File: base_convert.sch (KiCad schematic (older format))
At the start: 53 parts, among them SW1 SW_Push, SW10 SW_Push, SW11 SW_Push, SW12 SW_Push, SW13 SW_Push, SW14 SW_Push, SW15 SW_Push, SW16 SW_Push, SW17 SW_Push, SW18 SW_Push, SW19 SW_Push, SW2 SW_Push, SW20 SW_Push, SW21 SW_Push, SW22 SW_Push, SW23 SW_Push, SW24 SW_Push, SW25 SW_Push, SW26 SW_Push, SW27 SW_Push, SW28 SW_Push, SW29 SW_Push, SW3 SW_Push, SW30 SW_Push, SW31 SW_Push, SW32 SW_Push, SW4 SW_Push, SW5 SW_Push, SW6 SW_Push, SW7 SW_Push, SW8 SW_Push, SW9 SW_Push

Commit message: start schematic
getting there
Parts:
- removed AFF1, AFF2, AFF3, AFF4, AFF5: DA04-11, Displays_7-Segment:DA04-11SURKWA, symbol DA04-11
- removed D1, D10, D11, D12, D13, D14, D15, D16, D2, D3, D4, D5, D6, D7, D8, D9: LED, LEDs:LED_D3.0mm, symbol LED
- removed SW1, SW10, SW11, SW12, SW13, SW14, SW15, SW16, SW17, SW18, SW19, SW2, SW20, SW21, SW22, SW23, SW24, SW25, SW26, SW27, SW28, SW29, SW3, SW30, SW31, SW32, SW4, SW5, SW6, SW7, SW8, SW9: SW_Push, Buttons_Switches_SMD:SW_SPST_FSMSM, symbol SW_Push

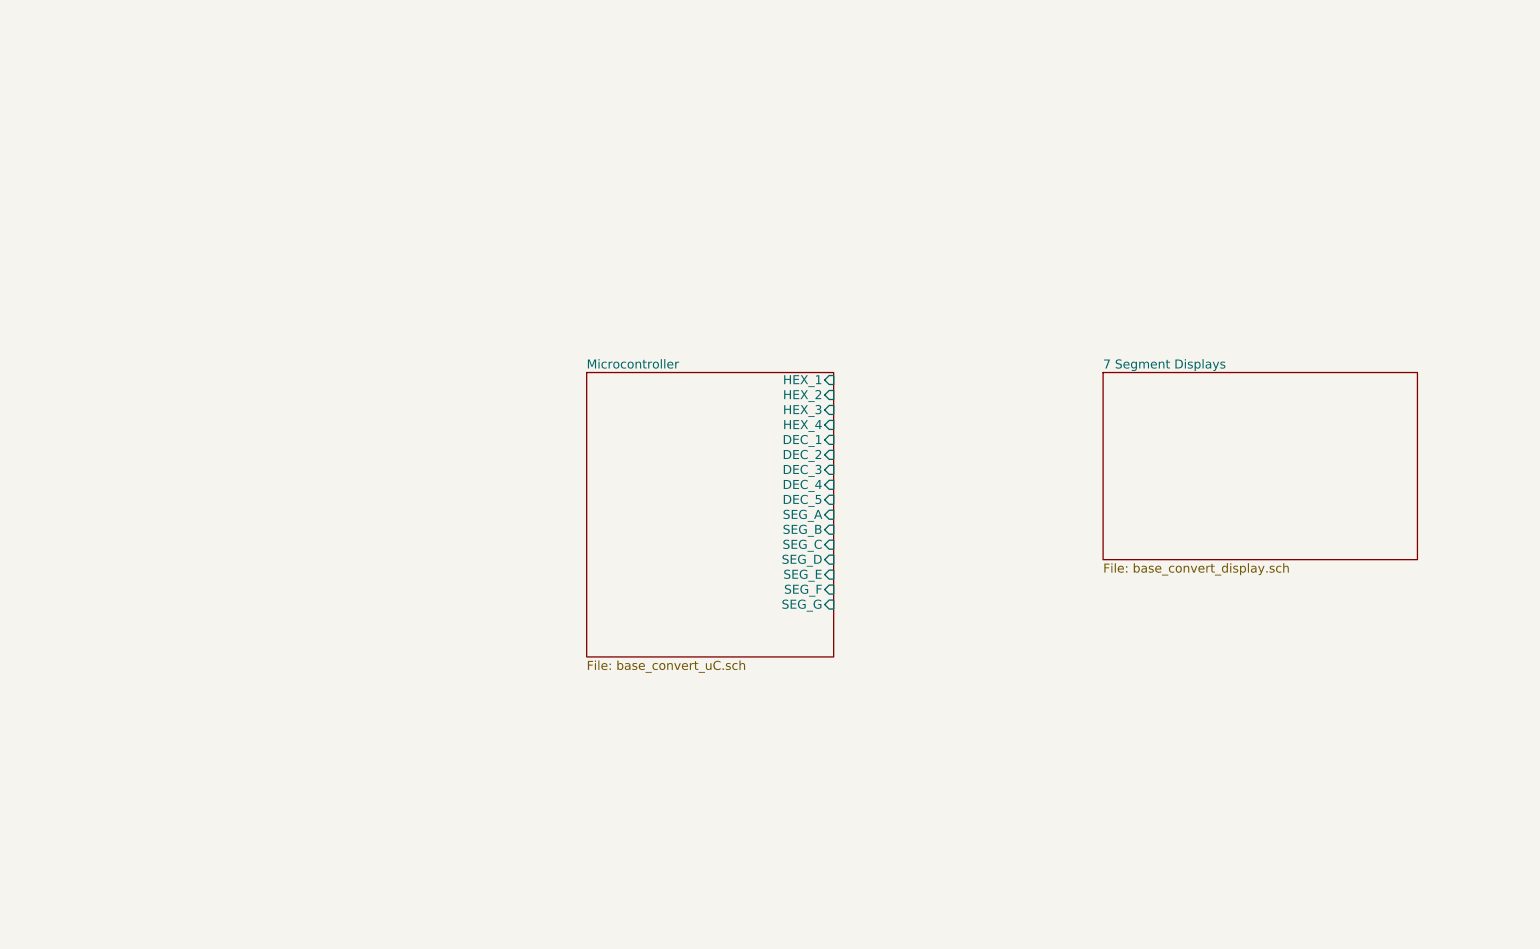
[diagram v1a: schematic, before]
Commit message: capture keypad inputs
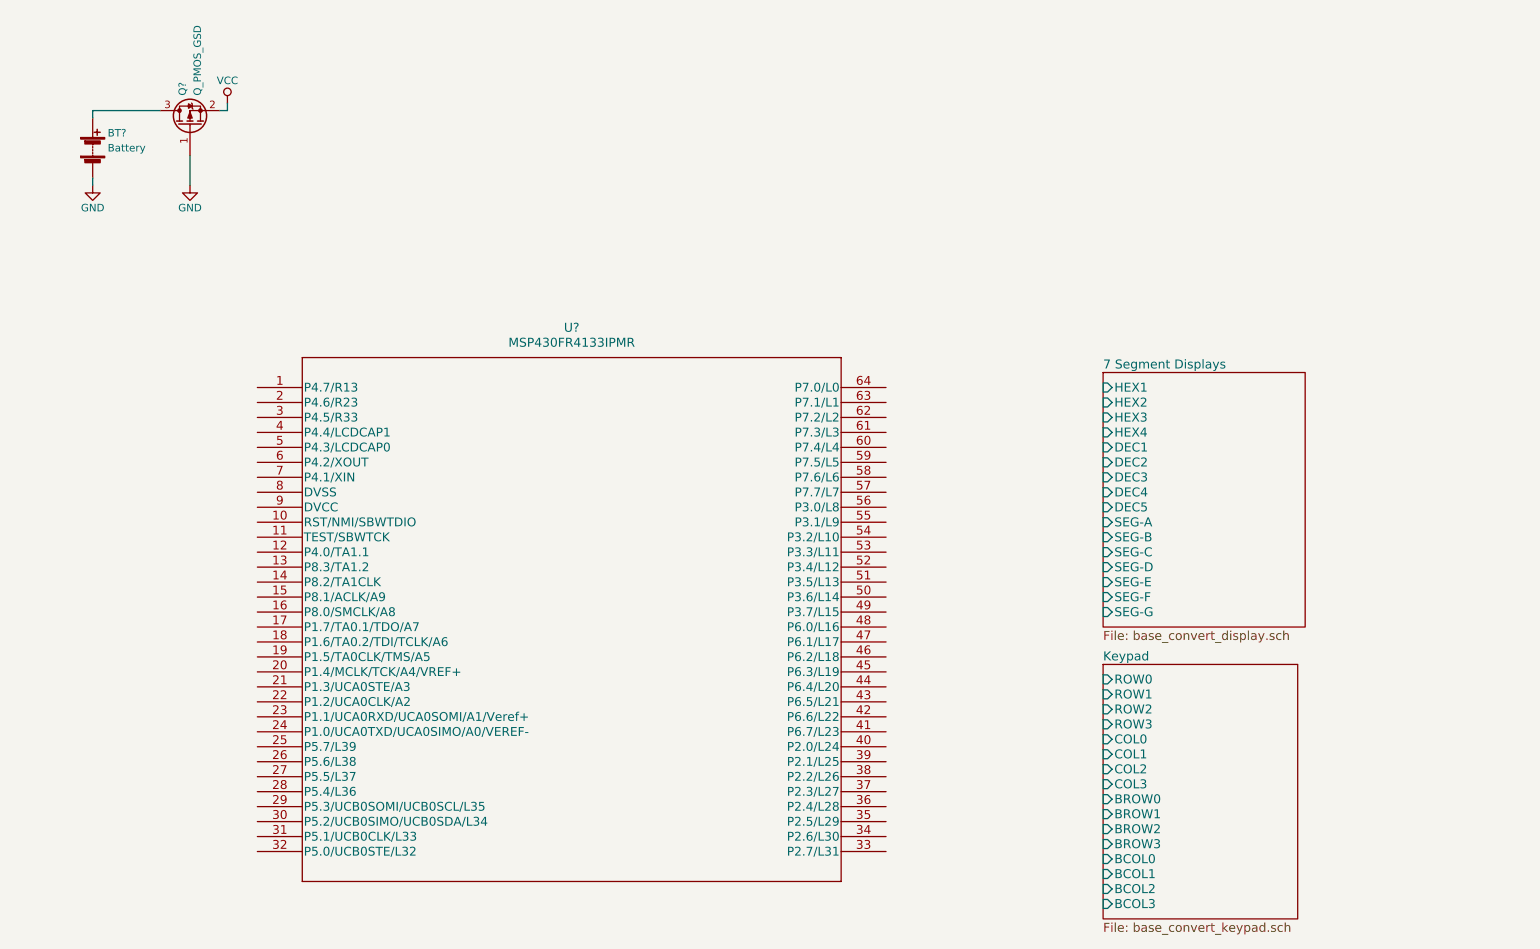
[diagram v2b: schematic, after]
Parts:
- added BT?: Battery, symbol Battery
- added Q?: Q_PMOS_GSD, symbol Q_PMOS_GSD
- added U?: MSP430FR4133IPMR, PM64, symbol MSP430FR4133IPMR
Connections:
- new net: BT?.1 (+), Q?.3 (D)
- new net GND: BT?.2 (-), Q?.1 (G)
- new net VCC: Q?.2 (S)
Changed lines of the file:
@@
 $EndDescr
 $Sheet
-S 4300 2850 1650 1900
-U 5AEA74A7
-F0 "Microcontroller" 60
-F1 "base_convert_uC.sch" 60
-F2 "SEG_A" I R 5950 3800 60
-F3 "SEG_B" I R 5950 3900 60
-F4 "SEG_C" I R 5950 4000 60
-F5 "SEG_D" I R 5950 4100 60
-F6 "SEG_E" I R 5950 4200 60
-F7 "SEG_F" I R 5950 4300 60
-F8 "SEG_G" I R 5950 4400 60
-F9 "HEX_1" I R 5950 2900 60
-F10 "HEX_2" I R 5950 3000 60
-F11 "HEX_3" I R 5950 3100 60
-F12 "HEX_4" I R 5950 3200 60
-F13 "DEC_1" I R 5950 3300 60
-F14 "DEC_2" I R 5950 3400 60
-F15 "DEC_3" I R 5950 3500 60
-F16 "DEC_4" I R 5950 3600 60
-F17 "DEC_5" I R 5950 3700 60
-$EndSheet
-$Sheet
-S 7750 2850 2100 1250
+S 7750 2850 1350 1700
 U 5AEA74C1
 F0 "7 Segment Displays" 60
 F1 "base_convert_display.sch" 60
+F2 "HEX1" I L 7750 2950 60
+F3 "HEX2" I L 7750 3050 60
+F4 "HEX3" I L 7750 3150 60
+F5 "HEX4" I L 7750 3250 60
+F6 "DEC1" I L 7750 3350 60
+F7 "DEC2" I L 7750 3450 60
+F8 "DEC3" I L 7750 3550 60
+F9 "DEC4" I L 7750 3650 60
+F10 "DEC5" I L 7750 3750 60
+F11 "SEG-A" I L 7750 3850 60
+F12 "SEG-B" I L 7750 3950 60
+F13 "SEG-C" I L 7750 4050 60
+F14 "SEG-D" I L 7750 4150 60
+F15 "SEG-E" I L 7750 4250 60
+F16 "SEG-F" I L 7750 4350 60
+F17 "SEG-G" I L 7750 4450 60
+$EndSheet
+$Comp
+L MSP430FR4133IPMR U?
+U 1 1 5AEBBA05
+P 2100 2950
+F 0 "U?" H 4200 3350 60  0000 C CNN
+F 1 "MSP430FR4133IPMR" H 4200 3250 60  0000 C CNN
+F 2 "PM64" H 4200 3190 60  0001 C CNN
+F 3 "" H 2100 2950 60  0000 C CNN
+	1    2100 2950
+	1    0    0    -1
+$EndComp
+$Comp
+L Battery BT?
+U 1 1 5AEC3A00
+P 1000 1350
+F 0 "BT?" H 1100 1450 50  0000 L CNN
+F 1 "Battery" H 1100 1350 50  0000 L CNN
+F 2 "" V 1000 1410 50  0001 C CNN
+F 3 "" V 1000 1410 50  0001 C CNN
+	1    1000 1350
+	1    0    0    -1
+$EndComp
+$Comp
+L GND #PWR?
+U 1 1 5AEC3D6F
+P 1000 1600
+F 0 "#PWR?" H 1000 1350 50  0001 C CNN
+F 1 "GND" H 1000 1450 50  0000 C CNN
+F 2 "" H 1000 1600 50  0001 C CNN
+F 3 "" H 1000 1600 50  0001 C CNN
+	1    1000 1600
+	1    0    0    -1
+$EndComp
+$Comp
+L Q_PMOS_GSD Q?
+U 1 1 5AEC4CC5
+P 1650 1200
+F 0 "Q?" H 1850 1250 50  0000 L CNN
+F 1 "Q_PMOS_GSD" H 1850 1150 50  0000 L CNN
+F 2 "" H 1850 1300 50  0001 C CNN
+F 3 "" H 1650 1200 50  0001 C CNN
+	1    1650 1200
+	0    -1   -1   0
+$EndComp
+Wire Wire Line
+	1000 1150 1000 1100
+Wire Wire Line
+	1000 1100 1450 1100
+Wire Wire Line
+	1000 1550 1000 1600
+$Comp
+L GND #PWR?
+U 1 1 5AEC5CE6
+P 1650 1600
+F 0 "#PWR?" H 1650 1350 50  0001 C CNN
+F 1 "GND" H 1650 1450 50  0000 C CNN
+F 2 "" H 1650 1600 50  0001 C CNN
+F 3 "" H 1650 1600 50  0001 C CNN
+	1    1650 1600
+	1    0    0    -1
+$EndComp
+Wire Wire Line
+	1650 1600 1650 1400
+$Comp
+L VCC #PWR?
+U 1 1 5AEC60F4
+P 1900 1050
+F 0 "#PWR?" H 1900 900 50  0001 C CNN
+F 1 "VCC" H 1900 1200 50  0000 C CNN
+F 2 "" H 1900 1050 50  0001 C CNN
+F 3 "" H 1900 1050 50  0001 C CNN
+	1    1900 1050
+	1    0    0    -1
+$EndComp
+Wire Wire Line
+	1850 1100 1900 1100
+Wire Wire Line
+	1900 1100 1900 1050
+$Sheet
+S 7750 4800 1300 1700
+U 5AEC7C6F
+F0 "Keypad" 60
+F1 "base_convert_keypad.sch" 60
+F2 "ROW0" I L 7750 4900 60
+F3 "ROW1" I L 7750 5000 60
+F4 "ROW2" I L 7750 5100 60
+F5 "ROW3" I L 7750 5200 60
+F6 "COL0" I L 7750 5300 60
+F7 "COL1" I L 7750 5400 60
+F8 "COL2" I L 7750 5500 60
+F9 "COL3" I L 7750 5600 60
+F10 "BROW0" I L 7750 5700 60
+F11 "BROW1" I L 7750 5800 60
+F12 "BROW2" I L 7750 5900 60
+F13 "BROW3" I L 7750 6000 60
+F14 "BCOL0" I L 7750 6100 60
+F15 "BCOL1" I L 7750 6200 60
+F16 "BCOL2" I L 7750 6300 60
+F17 "BCOL3" I L 7750 6400 60
 $EndSheet
 $EndSCHEMATC

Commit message: schematic captured, footprints complete
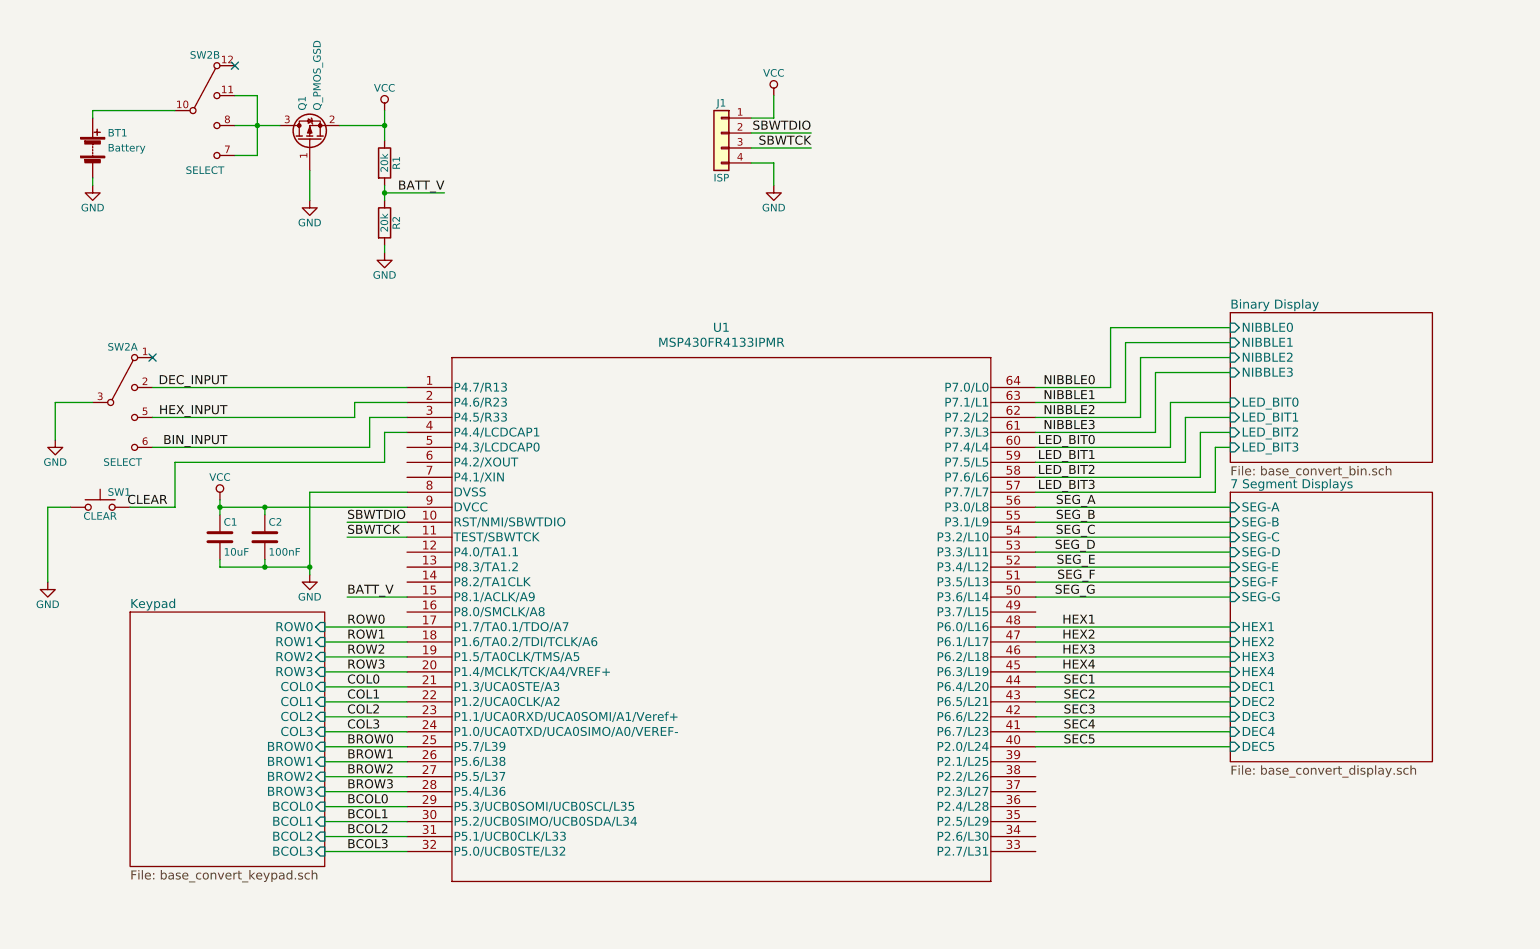
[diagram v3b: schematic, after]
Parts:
- added C1: 10uF, Capacitors_SMD:C_0805, symbol C
- added C2: 100nF, Capacitors_SMD:C_0805, symbol C
- added J1: ISP, Pin_Headers:Pin_Header_Straight_1x04_Pitch2.54mm, symbol Conn_01x04
- added R1, R2: 20k, Resistors_SMD:R_0805, symbol R
- added SW1: CLEAR, Buttons_Switches_THT:SW_PUSH_6mm, symbol SW_Push
- added SW2: SELECT, Switch_CK:DP4T_SS-24E06-TG5P, symbol SS-24E06-TG5P
- BT1: renamed from BT?; footprint (none) -> MPD:BC2AAPC; Description (none) -> NONE; Manufacture (none) -> NONE; Mfg Part Number (none) -> NONE; Package (none) -> NONE
- Q1: renamed from Q?; footprint (none) -> TO_SOT_Packages_SMD:SOT-23
- U1: renamed from U?; footprint PM64 -> Housings_QFP:LQFP-64_10x10mm_Pitch0.5mm
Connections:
- net GND: now also U1.8 (DVSS), C1.2, C2.2, J1.4 (Pin_4), R2.2, SW1.1, SW2.3 (COM)
- net VCC: now also U1.9 (DVCC), C1.1, C2.1, J1.1 (Pin_1), R1.1
- net DEC_INPUT: now reaches U1.1 (P4.7/R13)
- net DEC_INPUT: now also SW2.2 (B)
- net SBWTDIO: now reaches U1.10 (RST/NMI/SBWTDIO)
- net SBWTDIO: now also J1.2 (Pin_2)
- net SBWTCK: now reaches U1.11 (TEST/SBWTCK)
- net SBWTCK: now also J1.3 (Pin_3)
- net BATT_V: now reaches U1.15 (P8.1/ACLK/A9)
- net BATT_V: now also R1.2, R2.1
- net ROW0: now reaches U1.17 (P1.7/TA0.1/TDO/A7)
- net ROW1: now reaches U1.18 (P1.6/TA0.2/TDI/TCLK/A6)
- net ROW2: now reaches U1.19 (P1.5/TA0CLK/TMS/A5)
- net HEX_INPUT: now reaches U1.2 (P4.6/R23)
- net HEX_INPUT: now also SW2.5 (C)
- net ROW3: now reaches U1.20 (P1.4/MCLK/TCK/A4/VREF+)
- net COL0: now reaches U1.21 (P1.3/UCA0STE/A3)
- net COL1: now reaches U1.22 (P1.2/UCA0CLK/A2)
- net COL2: now reaches U1.23 (P1.1/UCA0RXD/UCA0SOMI/A1/Veref+)
- net COL3: now reaches U1.24 (P1.0/UCA0TXD/UCA0SIMO/A0/VEREF-)
- net BROW0: now reaches U1.25 (P5.7/L39)
- net BROW1: now reaches U1.26 (P5.6/L38)
- net BROW2: now reaches U1.27 (P5.5/L37)
- net BROW3: now reaches U1.28 (P5.4/L36)
- net BCOL0: now reaches U1.29 (P5.3/UCB0SOMI/UCB0SCL/L35)
- net BIN_INPUT: now reaches U1.3 (P4.5/R33)
- net BIN_INPUT: now also SW2.6 (D)
- net BCOL1: now reaches U1.30 (P5.2/UCB0SIMO/UCB0SDA/L34)
- net BCOL2: now reaches U1.31 (P5.1/UCB0CLK/L33)
- net BCOL3: now reaches U1.32 (P5.0/UCB0STE/L32)
- net CLEAR: now reaches U1.4 (P4.4/LCDCAP1)
- net CLEAR: now also SW1.2
- net SEC5: now reaches U1.40 (P2.0/L24)
- net SEC4: now reaches U1.41 (P6.7/L23)
- net SEC3: now reaches U1.42 (P6.6/L22)
- net SEC2: now reaches U1.43 (P6.5/L21)
- net SEC1: now reaches U1.44 (P6.4/L20)
- net HEX4: now reaches U1.45 (P6.3/L19)
- net HEX3: now reaches U1.46 (P6.2/L18)
- net HEX2: now reaches U1.47 (P6.1/L17)
- net HEX1: now reaches U1.48 (P6.0/L16)
- net SEG_G: now reaches U1.50 (P3.6/L14)
- net SEG_F: now reaches U1.51 (P3.5/L13)
- net SEG_E: now reaches U1.52 (P3.4/L12)
- net SEG_D: now reaches U1.53 (P3.3/L11)
- net SEG_C: now reaches U1.54 (P3.2/L10)
- net SEG_B: now reaches U1.55 (P3.1/L9)
- net SEG_A: now reaches U1.56 (P3.0/L8)
- net LED_BIT3: now reaches U1.57 (P7.7/L7)
- net LED_BIT2: now reaches U1.58 (P7.6/L6)
- net LED_BIT1: now reaches U1.59 (P7.5/L5)
- net LED_BIT0: now reaches U1.60 (P7.4/L4)
- net NIBBLE3: now reaches U1.61 (P7.3/L3)
- net NIBBLE2: now reaches U1.62 (P7.2/L2)
- net NIBBLE1: now reaches U1.63 (P7.1/L1)
- net NIBBLE0: now reaches U1.64 (P7.0/L0)
- net at BT1.1 (+): now also SW2.10 (COM); no longer Q1.3 (D)
- new net: Q1.3 (D), SW2.11 (B), SW2.7 (D), SW2.8 (C)
- no-connect marks 0 -> 2
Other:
- moved on the sheet: Q1, U1
